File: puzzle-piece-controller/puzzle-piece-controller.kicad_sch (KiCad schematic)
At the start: 10 parts, among them J1 POGO PINS, J2 OUTPUT_1, J4 BUTTON, J5 Conn_01x04_Socket, U1 MOUDLE-SEEEDUINO-XIAO-ESP32C3

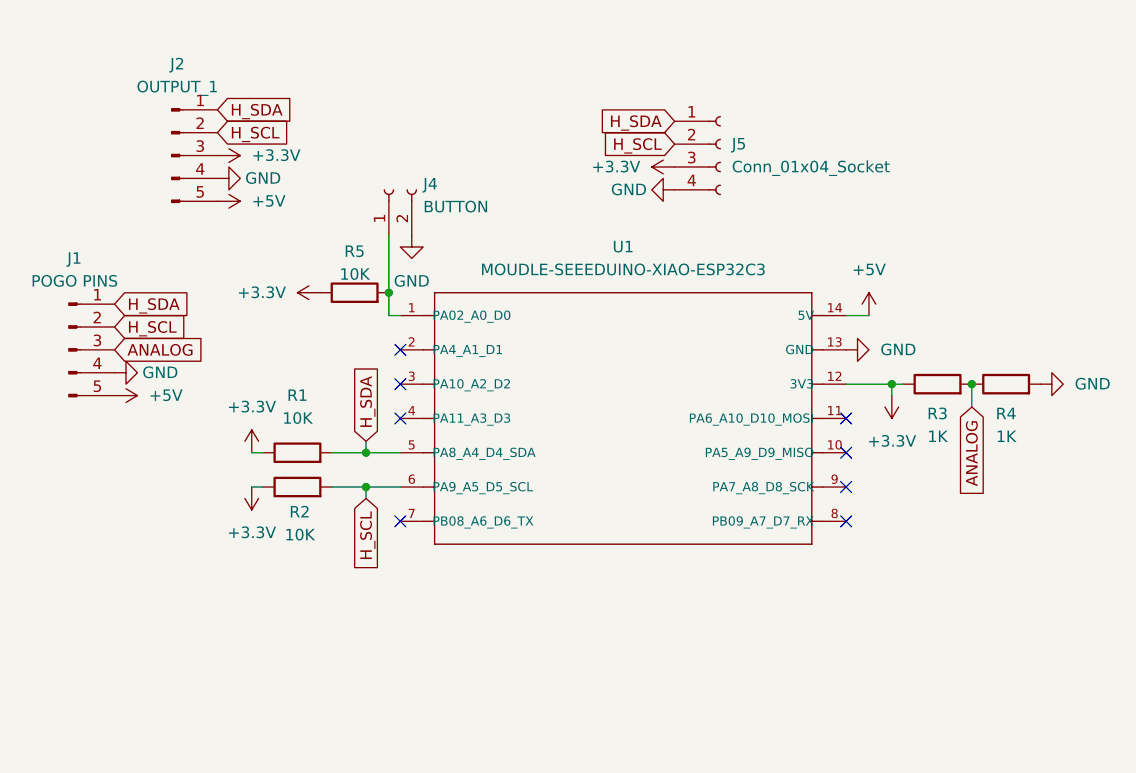
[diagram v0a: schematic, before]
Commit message: made battery controller singled sided and removed lipo
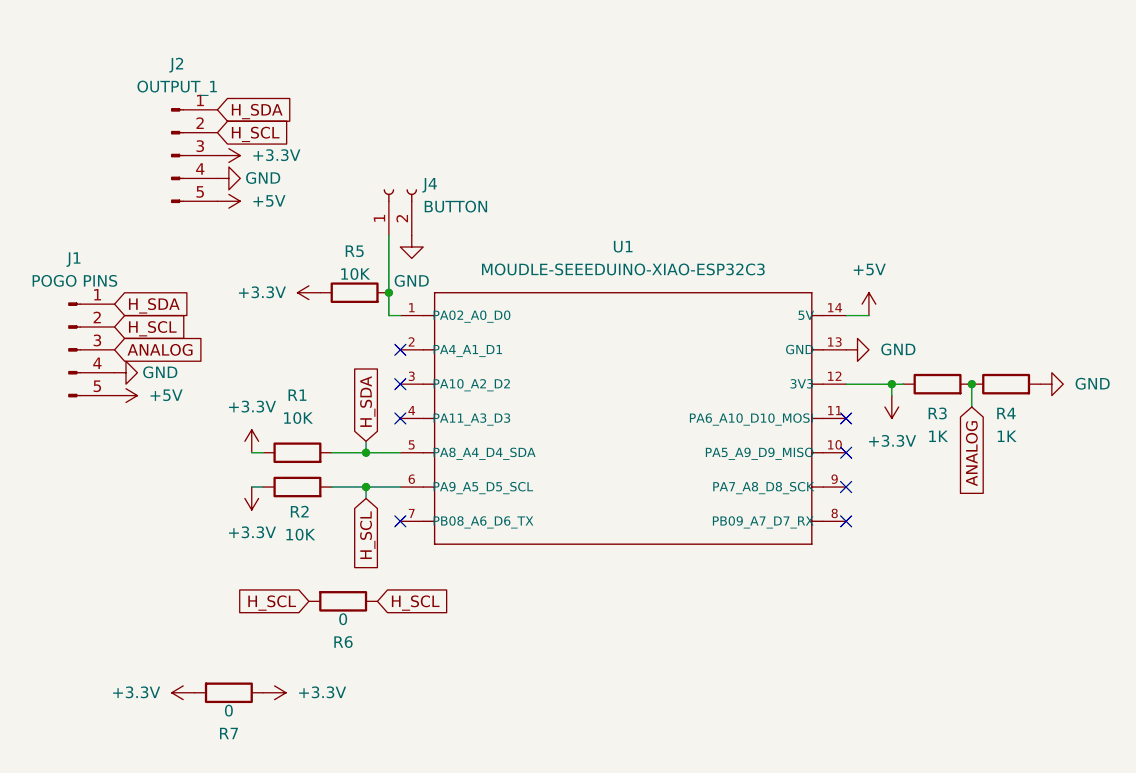
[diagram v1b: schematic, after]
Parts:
- removed J5: Conn_01x04_Socket, Connector_PinSocket_2.54mm:PinSocket_1x04_P2.54mm_Vertical, symbol Connector:Conn_01x04_Socket
- added R6, R7: 0, Resistor_SMD:R_1206_3216Metric_Pad1.30x1.75mm_HandSolder, symbol Device:R
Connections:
- net +3.3V: now also R7.1, R7.2
- net H_SCL: now also R6.1, R6.2

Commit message: made controller pcb single sided
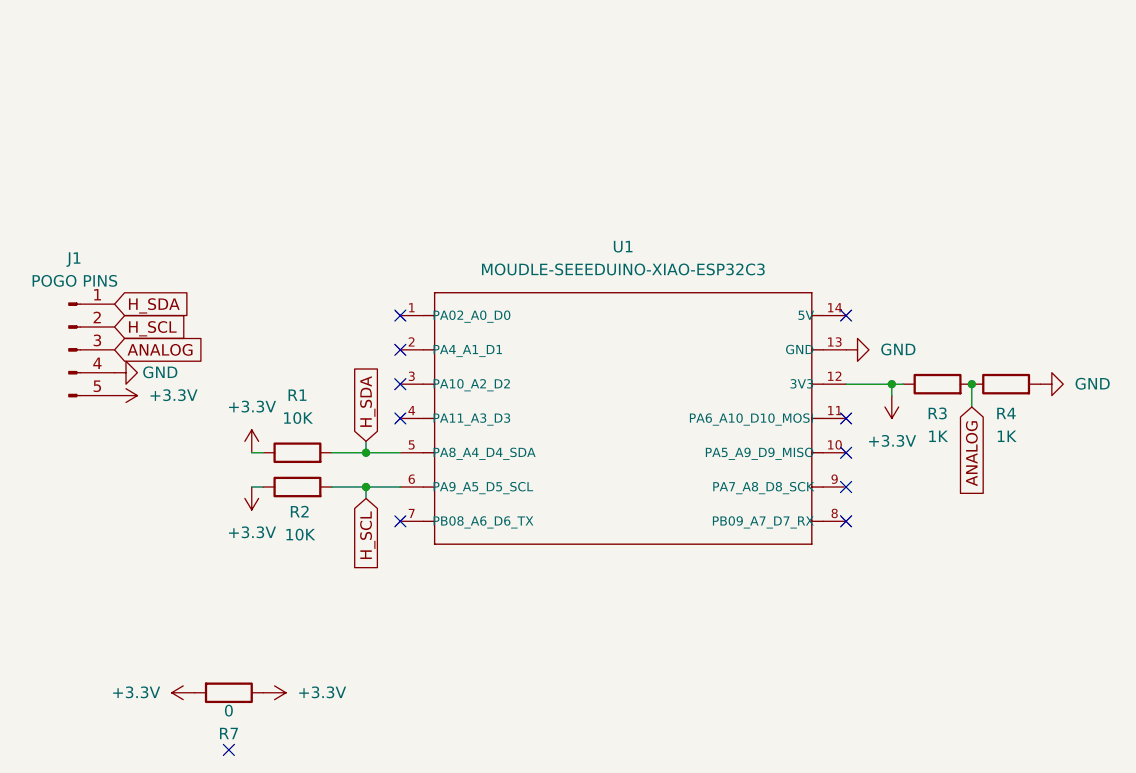
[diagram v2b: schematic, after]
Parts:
- removed J2: OUTPUT_1, Connector_PinSocket_2.54mm:PinSocket_1x05_P2.54mm_Vertical, symbol Connector:Conn_01x05_Pin
- removed J4: BUTTON, Connector_PinSocket_2.54mm:PinSocket_1x02_P2.54mm_Vertical, symbol Connector:Conn_01x02_Socket
- removed R5: 10K, Resistor_SMD:R_1206_3216Metric_Pad1.30x1.75mm_HandSolder, symbol Device:R
- removed R6: 0, Resistor_SMD:R_1206_3216Metric_Pad1.30x1.75mm_HandSolder, symbol Device:R
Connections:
- net +3.3V: now also J1.5 (Pin_5)
- net +5V: no longer names the net of U1.14 (5V)
- net +5V: no longer J1.5 (Pin_5)
- no-connect marks 8 -> 11

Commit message: add unrouted output throughholes to controller, and mounting holes
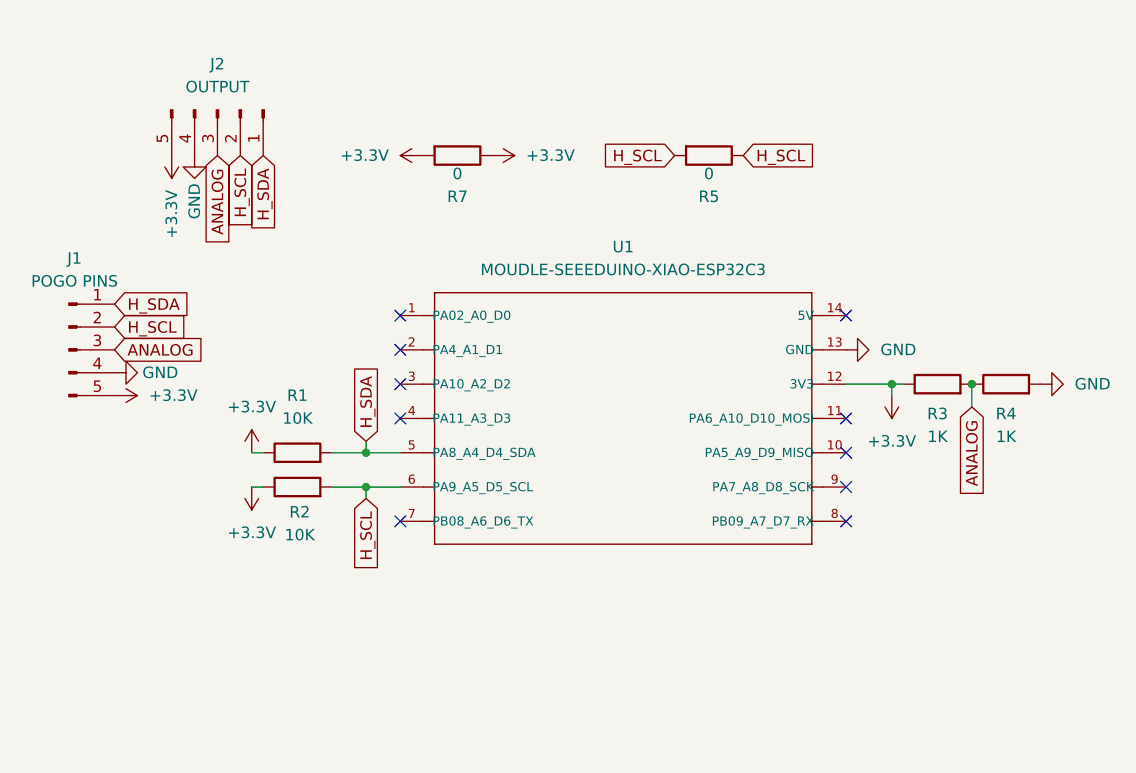
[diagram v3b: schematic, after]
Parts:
- added J2: OUTPUT, Connector_PinHeader_2.54mm:PinHeader_1x05_P2.54mm_Vertical, symbol Connector:Conn_01x05_Pin
- added R5: 0, Resistor_SMD:R_1206_3216Metric_Pad1.30x1.75mm_HandSolder, symbol Device:R
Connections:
- net +3.3V: now also J2.5 (Pin_5)
- net ANALOG: now also J2.3 (Pin_3)
- net GND: now also J2.4 (Pin_4)
- net H_SCL: now also J2.2 (Pin_2), R5.1, R5.2
- net H_SDA: now also J2.1 (Pin_1)
- no-connect marks 11 -> 10
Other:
- moved on the sheet: R7

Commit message: made puzzle-controller board double sided
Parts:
- added J3: 3.3V, Connector_PinSocket_2.54mm:PinSocket_1x01_P2.54mm_Vertical, symbol Connector:Conn_01x01_Socket
- added J4: GND, Connector_PinSocket_2.54mm:PinSocket_1x01_P2.54mm_Vertical, symbol Connector:Conn_01x01_Socket
- added J5: ANALOG, Connector_PinSocket_2.54mm:PinSocket_1x01_P2.54mm_Vertical, symbol Connector:Conn_01x01_Socket
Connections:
- net +3.3V: now also J3.1 (Pin_1)
- net ANALOG: now also J5.1 (Pin_1)
- net GND: now also J4.1 (Pin_1)

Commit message: current puzzle with attiny and pogo pins
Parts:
- removed J2: OUTPUT, Connector_PinHeader_2.54mm:PinHeader_1x05_P2.54mm_Vertical, symbol Connector:Conn_01x05_Pin
- removed J5: ANALOG, Connector_PinSocket_2.54mm:PinSocket_1x01_P2.54mm_Vertical, symbol Connector:Conn_01x01_Socket
- added J2: ANALOG, Connector_PinSocket_2.54mm:PinSocket_1x01_P2.54mm_Vertical, symbol Connector:Conn_01x01_Socket
- added J6: OUTPUT, Connector_PinSocket_2.54mm:PinSocket_1x04_P2.54mm_Vertical, symbol Connector:Conn_01x04_Socket
- U1: footprint xiao ESP32C3_PCB:MOUDLE14P-SMD-2.54-21X17.8MM -> fab:SeeedStudio_XIAO_ESP32C3
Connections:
- net +3.3V: now also J6.4 (Pin_4)
- net ANALOG: now also J2.1 (Pin_1)
- net GND: now also J6.3 (Pin_3)
- net H_SCL: now also J6.2 (Pin_2)
- net H_SDA: now also J6.1 (Pin_1)
